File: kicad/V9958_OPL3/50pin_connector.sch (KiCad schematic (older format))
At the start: 1 part, among them P5 CONN_02X25

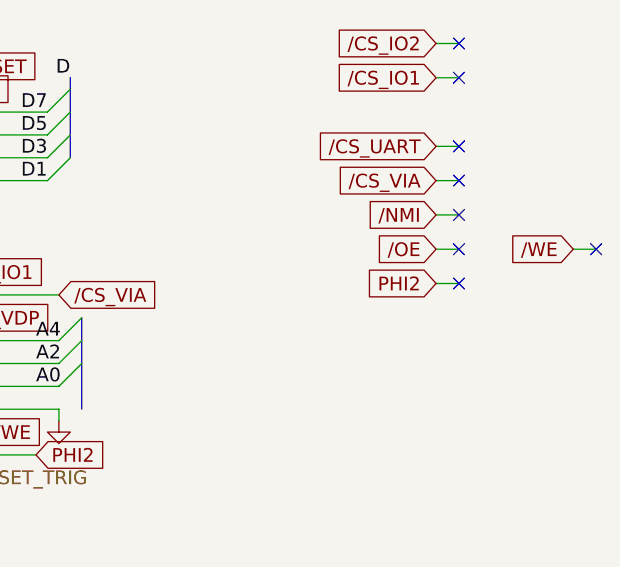
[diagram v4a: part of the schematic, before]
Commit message: generate OPL2 /CSW and /CSR by using PHI2 and RDY
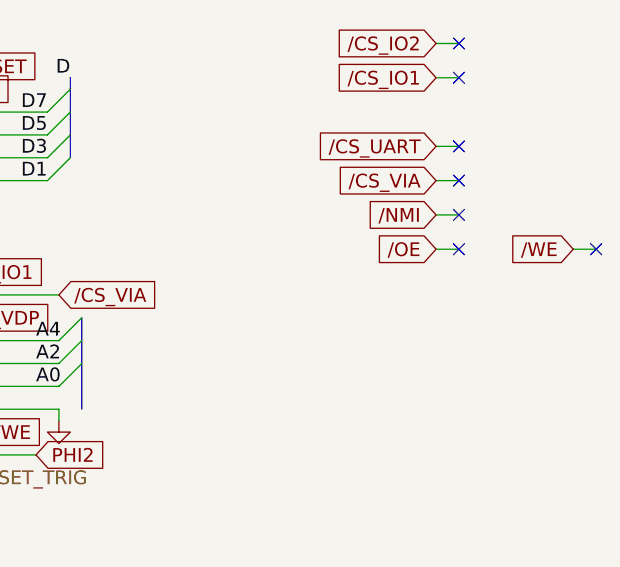
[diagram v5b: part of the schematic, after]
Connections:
- no-connect marks 16 -> 15
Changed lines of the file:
@@
 LIBS:yamaha_opl
 LIBS:rc4136
+LIBS:ttl_ieee
 LIBS:v9958-cache
 EELAYER 25 0
@@
 $EndComp
 $Comp
-L VCC #PWR018
+L VCC #PWR017
 U 1 1 54207202
 P 5200 2400
-F 0 "#PWR018" H 5200 2500 30  0001 C CNN
+F 0 "#PWR017" H 5200 2500 30  0001 C CNN
 F 1 "VCC" H 5200 2500 30  0000 C CNN
 F 2 "" H 5200 2400 60  0000 C CNN
@@
 	4750 3950 5300 3950
 $Comp
-L GND #PWR019
+L GND #PWR018
 U 1 1 54207240
 P 4700 4100
-F 0 "#PWR019" H 4700 4100 30  0001 C CNN
+F 0 "#PWR018" H 4700 4100 30  0001 C CNN
 F 1 "GND" H 4700 4030 30  0001 C CNN
 F 2 "" H 4700 4100 60  0000 C CNN
@@
 	4700 4050 5300 4050
 $Comp
-L GND #PWR020
+L GND #PWR019
 U 1 1 54207248
 P 6350 4100
-F 0 "#PWR020" H 6350 4100 30  0001 C CNN
+F 0 "#PWR019" H 6350 4100 30  0001 C CNN
 F 1 "GND" H 6350 4030 30  0001 C CNN
 F 2 "" H 6350 4100 60  0000 C CNN
@@
 A5
 $Comp
-L GND #PWR021
+L GND #PWR020
 U 1 1 5436D639
 P 5250 5150
-F 0 "#PWR021" H 5250 5150 30  0001 C CNN
+F 0 "#PWR020" H 5250 5150 30  0001 C CNN
 F 1 "GND" H 5250 5080 30  0001 C CNN
 F 2 "" H 5250 5150 60  0000 C CNN
@@
 Connection ~ 5250 4950
 $Comp
-L VCC #PWR022
+L VCC #PWR021
 U 1 1 5436D6BC
 P 5950 4550
-F 0 "#PWR022" H 5950 4650 30  0001 C CNN
+F 0 "#PWR021" H 5950 4650 30  0001 C CNN
 F 1 "VCC" H 5950 4650 30  0000 C CNN
 F 2 "" H 5950 4550 60  0000 C CNN
@@
 Connection ~ 5950 4650
 $Comp
-L VCC #PWR023
+L VCC #PWR022
 U 1 1 5436D806
 P 5150 4550
-F 0 "#PWR023" H 5150 4650 30  0001 C CNN
+F 0 "#PWR022" H 5150 4650 30  0001 C CNN
 F 1 "VCC" H 5150 4650 30  0000 C CNN
 F 2 "" H 5150 4550 60  0000 C CNN
@@
 RESET_TRIG
 $Comp
-L GND #PWR024
+L GND #PWR023
 U 1 1 54BC2AE5
 P 4700 4300
-F 0 "#PWR024" H 4700 4300 30  0001 C CNN
+F 0 "#PWR023" H 4700 4300 30  0001 C CNN
 F 1 "GND" H 4700 4230 30  0001 C CNN
 F 2 "" H 4700 4300 60  0000 C CNN
@@
 	8000 3350 8100 3350
 NoConn ~ 8100 3350
-Text GLabel 8000 3500 0    60   Input ~ 0
-PHI2
-Wire Wire Line
-	8000 3500 8100 3500
-NoConn ~ 8100 3500
 Text GLabel 8000 3050 0    60   Input ~ 0
 /CS_VIA
